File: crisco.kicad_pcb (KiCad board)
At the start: 2 copper layers, 213.4 x 38.1 mm, 44 parts, among them J1 LED, J2 OLED, U1 ProMicro

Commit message: reset switch
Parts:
- added RST: SW_Push, Button_Switch_SMD:SW_SPST_B3U-1000P, F.Cu at (42.9, 76.1)
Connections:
- U1 pad 22: Net-(U1-Pad22) -> rst
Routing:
- net rst: track 0.00 -> 4.99 mm
- net GND: track 75.9 -> 80.5 mm
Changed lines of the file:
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@@
     (thickness 1.6)
     (drawings 9)
-    (tracks 302)
+    (tracks 306)
     (zones 0)
-    (modules 44)
+    (modules 45)
     (nets 43)
   )
@@
   (net 40 sda)
   (net 41 scl)
-  (net 42 "Net-(U1-Pad22)")
+  (net 42 rst)
   (net_class Default "これはデフォルトのネット クラスです。"
     (clearance 0.2)
@@
     (add_net "Net-(U1-Pad12)")
     (add_net "Net-(U1-Pad2)")
-    (add_net "Net-(U1-Pad22)")
     (add_net "Net-(U1-Pad24)")
     (add_net VCC)
@@
     (add_net row0)
     (add_net row1)
+    (add_net rst)
     (add_net scl)
     (add_net sda)
+  )
+  (module Button_Switch_SMD:SW_SPST_B3U-1000P (layer F.Cu)
+    (at 42.926 76.073 90)
+    (descr "Ultra-small-sized Tactile Switch with High Contact Reliability, Top-actuated Model, without Ground Terminal, without Boss")
+    (tags "Tactile Switch")
+    (attr smd)
+    (fp_text reference RST (at 0 -2.286 90) (layer F.SilkS)
+      (effects (font (size 1 1) (thickness 0.15)))
+    )
+    (fp_text value SW_Push (at 0 2.5 90) (layer F.Fab)
+      (effects (font (size 1 1) (thickness 0.15)))
+    )
+    (fp_circle (center 0 0) (end 0.75 0) (layer F.Fab) (width 0.1))
+    (fp_line (start -1.5 1.25) (end -1.5 -1.25) (layer F.Fab) (width 0.1))
+    (fp_line (start 1.5 1.25) (end -1.5 1.25) (layer F.Fab) (width 0.1))
+    (fp_line (start 1.5 -1.25) (end 1.5 1.25) (layer F.Fab) (width 0.1))
+    (fp_line (start -1.5 -1.25) (end 1.5 -1.25) (layer F.Fab) (width 0.1))
+    (fp_line (start 1.65 -1.4) (end 1.65 -1.1) (layer F.SilkS) (width 0.12))
+    (fp_line (start -1.65 -1.4) (end 1.65 -1.4) (layer F.SilkS) (width 0.12))
+    (fp_line (start -1.65 -1.1) (end -1.65 -1.4) (layer F.SilkS) (width 0.12))
+    (fp_line (start 1.65 1.4) (end 1.65 1.1) (layer F.SilkS) (width 0.12))
+    (fp_line (start -1.65 1.4) (end 1.65 1.4) (layer F.SilkS) (width 0.12))
+    (fp_line (start -1.65 1.1) (end -1.65 1.4) (layer F.SilkS) (width 0.12))
+    (fp_line (start -2.4 -1.65) (end -2.4 1.65) (layer F.CrtYd) (width 0.05))
+    (fp_line (start 2.4 -1.65) (end -2.4 -1.65) (layer F.CrtYd) (width 0.05))
+    (fp_line (start 2.4 1.65) (end 2.4 -1.65) (layer F.CrtYd) (width 0.05))
+    (fp_line (start -2.4 1.65) (end 2.4 1.65) (layer F.CrtYd) (width 0.05))
+    (fp_text user %R (at 0 0.127 90) (layer F.Fab)
+      (effects (font (size 1 1) (thickness 0.15)))
+    )
+    (pad 1 smd rect (at -1.7 0 90) (size 0.9 1.7) (layers F.Cu F.Paste F.Mask)
+      (net 42 rst))
+    (pad 2 smd rect (at 1.7 0 90) (size 0.9 1.7) (layers F.Cu F.Paste F.Mask)
+      (net 9 GND))
+    (model ${KISYS3DMOD}/Button_Switch_SMD.3dshapes/SW_SPST_B3U-1000P.wrl
+      (at (xyz 0 0 0))
+      (scale (xyz 1 1 1))
+      (rotate (xyz 0 0 0))
+    )
   )
   (module MX_Alps_Hybrid:MXOnly-1U-NoLED (layer F.Cu)
@@
       (net 11 VCC))
     (pad 22 thru_hole circle (at -8.89 -7.62 270) (size 1.7526 1.7526) (drill 1.0922) (layers *.Cu *.SilkS *.Mask)
-      (net 42 "Net-(U1-Pad22)"))
+      (net 42 rst))
     (pad 23 thru_hole circle (at -11.43 -7.62 270) (size 1.7526 1.7526) (drill 1.0922) (layers *.Cu *.SilkS *.Mask)
       (net 9 GND))
@@
   (segment (start 33.29999 105.76501) (end 26.554598 105.76501) (width 0.25) (layer B.Cu) (net 9))
   (segment (start 34.925 104.14) (end 33.29999 105.76501) (width 0.25) (layer B.Cu) (net 9))
+  (segment (start 42.60275 74.77125) (end 42.926 74.448) (width 0.25) (layer F.Cu) (net 9))
+  (segment (start 38.4175 74.77125) (end 42.60275 74.77125) (width 0.25) (layer F.Cu) (net 9))
   (segment (start 24.378801 73.432551) (end 23.1775 72.23125) (width 0.25) (layer B.Cu) (net 10))
   (segment (start 44.323 78.898824) (end 38.856727 73.432551) (width 0.25) (layer B.Cu) (net 10))
@@
   (segment (start 29.845 104.14) (end 28.669999 105.315001) (width 0.25) (layer B.Cu) (net 41))
   (segment (start 38.4175 77.31125) (end 38.1 77.31125) (width 0.5) (layer B.Cu) (net 42))
+  (segment (start 42.53925 77.31125) (end 42.926 77.698) (width 0.25) (layer F.Cu) (net 42))
+  (segment (start 38.4175 77.31125) (end 42.53925 77.31125) (width 0.25) (layer F.Cu) (net 42))
 )

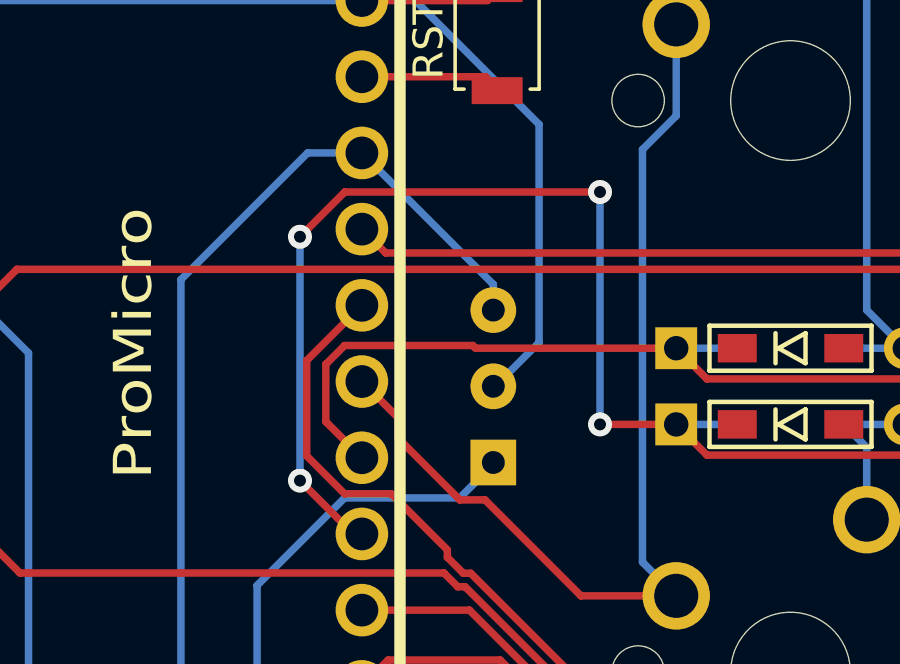
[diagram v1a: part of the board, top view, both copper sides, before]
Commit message: update vias
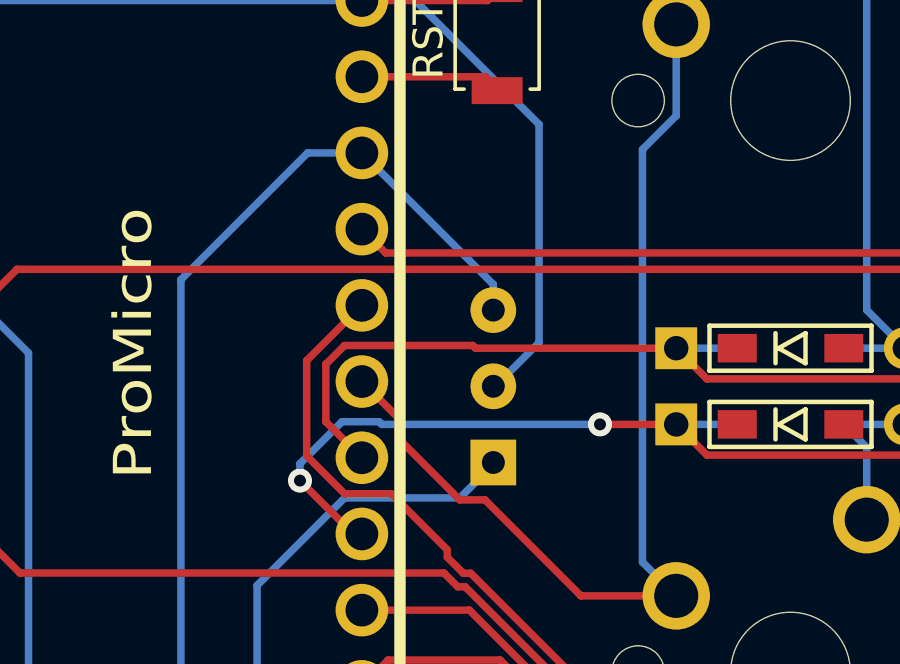
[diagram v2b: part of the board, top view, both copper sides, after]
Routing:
- net row1: track 231.3 -> 216.0 mm, vias 4 -> 2
